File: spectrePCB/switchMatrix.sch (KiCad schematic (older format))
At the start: 256 parts

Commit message: finished capslock key and pin mapping. Rev1 done
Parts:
- added U?: TS3A24159DGSR, Package_SO:TSSOP-10_3x3mm_P0.5mm, symbol Analog_Switch:TS3A24159DGSR
- added U? (x2): 74LVC2G08, symbol 74xGxx:74LVC2G08
- added U?: CD74HC73M96, symbol MyComponents:CD74HC73M96
- MX?: value delete -> ctrl
- MX?: value menu -> del
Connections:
- net COL15 is gone; now on net COL13: MX?.1 (COL), MX?.1 (COL)
- net COL16 is gone; now on net COL14: MX?.1 (COL)
- net COL0: now also U?.1
- net COL10: now also MX?.1 (COL); no longer MX?.1 (COL)
- net COL11: now also MX?.1 (COL)
- net COL12: now also MX?.1 (COL), MX?.1 (COL), MX?.1 (COL); no longer MX?.1 (COL)
- net COL13: no longer MX?.1 (COL), MX?.1 (COL), MX?.1 (COL)
- net COL14: no longer MX?.1 (COL)
- net COL5: now also MX?.1 (COL)
- net COL6: no longer MX?.1 (COL)
- net COL9: now also MX?.1 (COL)
- net L+: now also U?.6; no longer R?.1
- net L-: no longer D?.1 (K), D?.1 (K), D?.1 (K), D?.1 (K), D?.1 (K), D?.1 (K), D?.1 (K), D?.1 (K), D?.1 (K), D?.1 (K), D?.1 (K), D?.1 (K), D?.1 (K)
- net ROW2: now also U?.2
- net at R?.2: now also U?.3; no longer D?.2 (A)
- new net: U?.7, U?.8
- new net: D?.2 (A), R?.1
- new net GND: U?.4 (GND), U?.4 (GND)
- new net ROW3: D?.1 (K), D?.1 (K), D?.1 (K), D?.1 (K), D?.1 (K), D?.1 (K), D?.1 (K), D?.1 (K), D?.1 (K), D?.1 (K), D?.1 (K), D?.1 (K), D?.1 (K)
- new net VCC: U?.8 (VCC), U?.8 (VCC)
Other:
- moved on the sheet: D?, MX?, R?

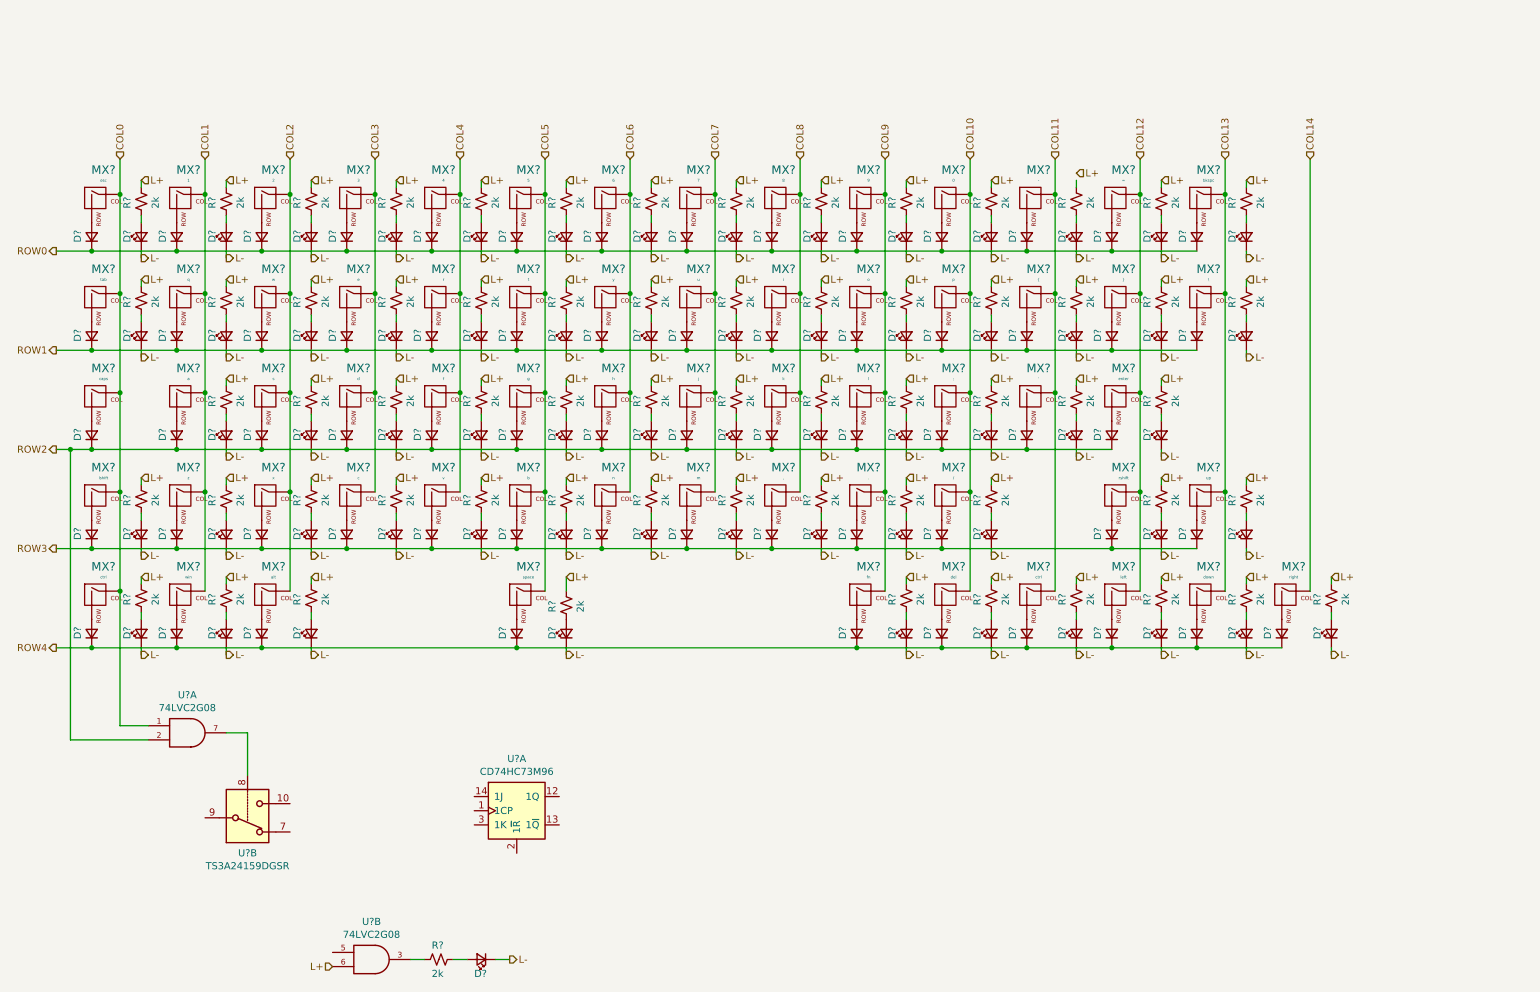
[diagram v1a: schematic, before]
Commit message: fixed big decoup cap not being big
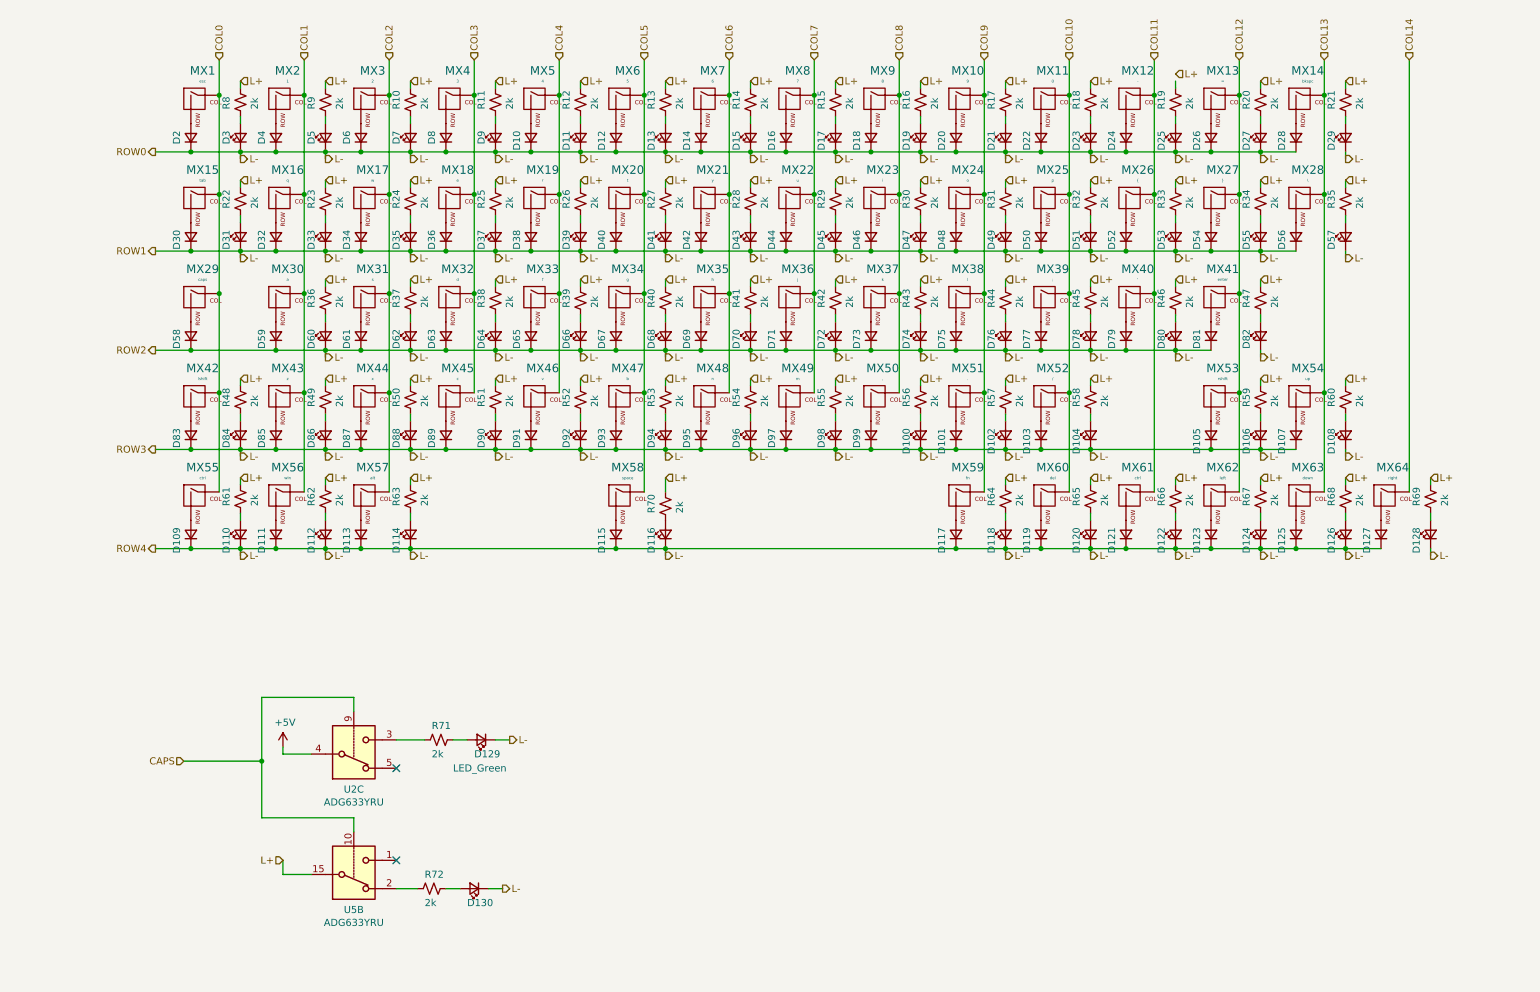
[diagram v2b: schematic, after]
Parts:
- removed U?: TS3A24159DGSR, Package_SO:TSSOP-10_3x3mm_P0.5mm, symbol Analog_Switch:TS3A24159DGSR
- removed U? (x2): 74LVC2G08, symbol 74xGxx:74LVC2G08
- removed U?: CD74HC73M96, symbol MyComponents:CD74HC73M96
- added D129: LED_Green, symbol Device:LED_Small
- added R71: 2k, symbol Device:R_Small_US
- added U2, U5: ADG633YRU, Package_SO:TSSOP-20_4.4x6.5mm_P0.65mm, symbol Analog_Switch:ADG633YRU
- gave numbers to parts that had none: 256
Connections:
- net ROW0 is gone; now on net L-: D10.1 (K), D12.1 (K), D14.1 (K), D16.1 (K), D18.1 (K), D2.1 (K), D20.1 (K), D22.1 (K), D24.1 (K), D26.1 (K), D28.1 (K), D4.1 (K), D6.1 (K), D8.1 (K)
- net ROW1 is gone; now on net L-: D30.1 (K), D32.1 (K), D34.1 (K), D36.1 (K), D38.1 (K), D40.1 (K), D42.1 (K), D44.1 (K), D46.1 (K), D48.1 (K), D50.1 (K), D52.1 (K), D54.1 (K), D56.1 (K)
- net ROW2 is gone; now on net L-: D58.1 (K), D59.1 (K), D61.1 (K), D63.1 (K), D65.1 (K), D67.1 (K), D69.1 (K), D71.1 (K), D73.1 (K), D75.1 (K), D77.1 (K), D79.1 (K), D81.1 (K)
- net ROW3 is gone; now on net L-: D101.1 (K), D103.1 (K), D105.1 (K), D107.1 (K), D83.1 (K), D85.1 (K), D87.1 (K), D89.1 (K), D91.1 (K), D93.1 (K), D95.1 (K), D97.1 (K), D99.1 (K)
- net ROW4 is gone; now on net L-: D109.1 (K), D111.1 (K), D113.1 (K), D115.1 (K), D117.1 (K), D119.1 (K), D121.1 (K), D123.1 (K), D125.1 (K), D127.1 (K)
- net L+: now also U5.15
- net L-: now also D129.1 (K)
- net at R72.2: now also U5.2
- new net: D129.2 (A), R71.1
- new net: R71.2, U2.3
- new net +5V: U2.4
- new net CAPS: U2.9, U5.10
- no-connect marks 0 -> 2
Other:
- moved on the sheet: D10, D100, D101, D102, D103, D104, D105, D106, D107, D108, D109, D11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

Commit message: added footprints to components
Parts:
- D10, D101, D103, D105, D107, D109, D111, D113, D115, D117, D119, D12, D121, D123, D125, D127, D14, D16, D18, D2, D20, D22, D24, D26, D28, D30, D32, D34, D36, D38, D4, D40, D42, D44, D46, D48, D50, D52, D54, D56, D58, D59, D6, D61, D63, D65, D67, D69, D71, D73, D75, D77, D79, D8, D81, D83, D85, D87, D89, D91, D93, D95, D97, D99: footprint (none) -> Diode_SMD:D_0603_1608Metric
- D100, D102, D104, D106, D108, D11, D110, D112, D114, D116, D118, D120, D122, D124, D126, D128, D129, D13, D130, D15, D17, D19, D21, D23, D25, D27, D29, D3, D31, D33, D35, D37, D39, D41, D43, D45, D47, D49, D5, D51, D53, D55, D57, D60, D62, D64, D66, D68, D7, D70, D72, D74, D76, D78, D80, D82, D84, D86, D88, D9, D90, D92, D94, D96, D98: footprint (none) -> LED_SMD:LED_0603_1608Metric
- MX1, MX10, MX11, MX12, MX13, MX16, MX17, MX18, MX19, MX2, MX20, MX21, MX22, MX23, MX24, MX25, MX26, MX27, MX3, MX30, MX31, MX32, MX33, MX34, MX35, MX36, MX37, MX38, MX39, MX4, MX40, MX43, MX44, MX45, MX46, MX47, MX48, MX49, MX5, MX50, MX51, MX52, MX54, MX6, MX62, MX63, MX64, MX7, MX8, MX9: footprint (none) -> MX_Alps_Hybrid:MX-1U-NoLED
- MX14: footprint (none) -> MX_Alps_Hybrid:MX-2U-NoLED
- MX15, MX28: footprint (none) -> MX_Alps_Hybrid:MX-1.5U-NoLED
- MX29: footprint (none) -> MX_Alps_Hybrid:MX-1.75U-NoLED
- MX41, MX42: footprint (none) -> MX_Alps_Hybrid:MX-2.25U-NoLED
- MX53: footprint (none) -> MX_Alps_Hybrid:MX-2.75U-NoLED
- MX55, MX56, MX57, MX59, MX60, MX61: footprint (none) -> MX_Alps_Hybrid:MX-1.25U-NoLED
- MX58: footprint (none) -> MX_Alps_Hybrid:MX-6.25U-NoLED
- R10, R11, R12, R13, R14, R15, R16, R17, R18, R19, R20, R21, R22, R23, R24, R25, R26, R27, R28, R29, R30, R31, R32, R33, R34, R35, R36, R37, R38, R39, R40, R41, R42, R43, R44, R45, R46, R47, R48, R49, R50, R51, R52, R53, R54, R55, R56, R57, R58, R59, R60, R61, R62, R63, R64, R65, R66, R67, R68, R69, R70, R71, R72, R8, R9: footprint (none) -> Resistor_SMD:R_0201_0603Metric

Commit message: dove into the rats nest. I regret everything
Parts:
- MX55: value ctrl -> ctrlL
- MX61: value ctrl -> ctrlR
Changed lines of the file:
@@
 P 8400 4250
 F 0 "MX61" H 8433 4473 60  0000 C CNN
-F 1 "ctrl" H 8433 4399 20  0000 C CNN
+F 1 "ctrlR" H 8433 4399 20  0000 C CNN
 F 2 "MX_Alps_Hybrid:MX-1.25U-NoLED" H 7775 4225 60  0001 C CNN
 F 3 "" H 7775 4225 60  0001 C CNN
@@
 P 1800 4250
 F 0 "MX55" H 1833 4473 60  0000 C CNN
-F 1 "ctrl" H 1833 4399 20  0000 C CNN
+F 1 "ctrlL" H 1833 4399 20  0000 C CNN
 F 2 "MX_Alps_Hybrid:MX-1.25U-NoLED" H 1175 4225 60  0001 C CNN
 F 3 "" H 1175 4225 60  0001 C CNN
@@
 	1    0    0    -1
 $EndComp
-Text HLabel 6900 2000 2    50   Input ~ 0
-L+
 Text HLabel 6900 2550 2    50   Output ~ 0
 L-
@@
 NoConn ~ 3200 6150
 NoConn ~ 3200 6800
+Text HLabel 6900 2000 2    50   Input ~ 0
+L+
 $EndSCHEMATC

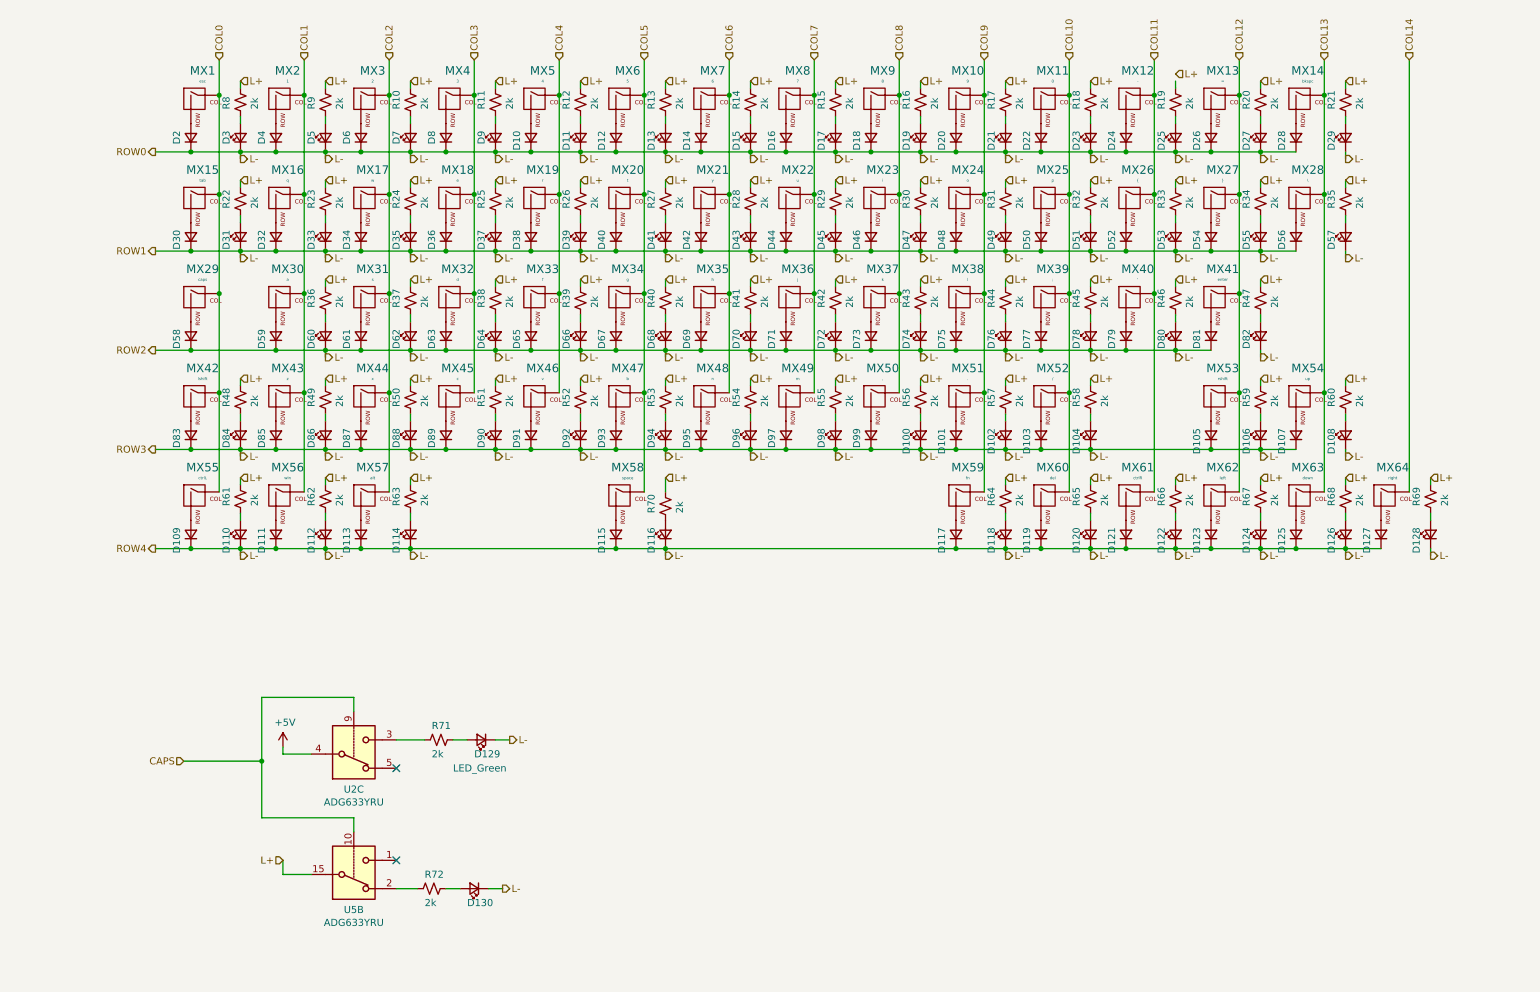
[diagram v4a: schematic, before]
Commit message: placed resistors, added edges, fixing GND net
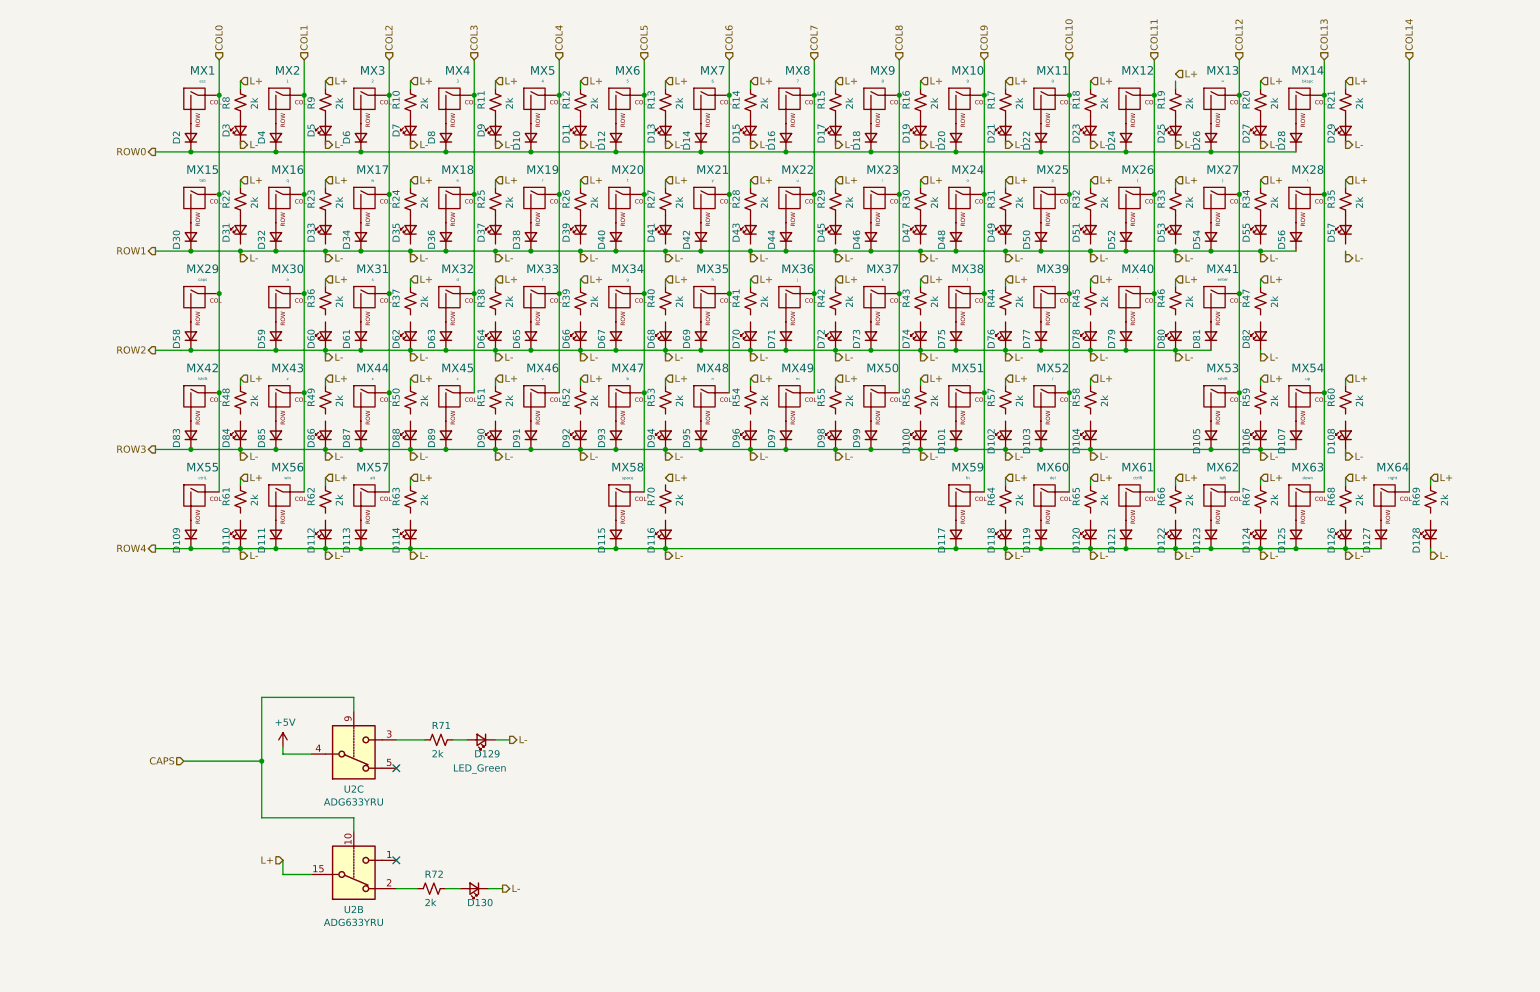
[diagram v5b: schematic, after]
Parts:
- R10, R11, R12, R13, R14, R15, R16, R17, R18, R19, R20, R21, R22, R23, R24, R25, R26, R27, R28, R29, R30, R31, R32, R33, R34, R35, R36, R37, R38, R39, R40, R41, R42, R43, R44, R45, R46, R47, R48, R49, R50, R51, R52, R53, R54, R55, R56, R57, R58, R59, R60, R61, R62, R63, R64, R65, R66, R67, R68, R69, R70, R71, R72, R8, R9: footprint Resistor_SMD:R_0201_0603Metric -> Resistor_SMD:R_0603_1608Metric
- renumbered U5 to U2
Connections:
- net L+: no longer R70.1
- net L-: no longer D10.1 (K), D12.1 (K), D14.1 (K), D16.1 (K), D18.1 (K), D2.1 (K), D20.1 (K), D22.1 (K), D24.1 (K), D26.1 (K), D28.1 (K), D31.1 (K), D33.1 (K), D35.1 (K), D37.1 (K), D39.1 (K), D4.1 (K), D41.1 (K), D43.1 (K), D45.1 (K), D47.1 (K), D49.1 (K), D51.1 (K), D53.1 (K), D55.1 (K), D57.1 (K), D6.1 (K), D8.1 (K)
- net at D84.2 (A): no longer R48.2
- net at D110.2 (A): no longer R61.2
- net at D60.2 (A): no longer R36.2
- net at D86.2 (A): no longer R49.2
- net at D112.2 (A): no longer R62.2
- net at D62.2 (A): no longer R37.2
- net at D88.2 (A): no longer R50.2
- net at D114.2 (A): no longer R63.2
- net at D64.2 (A): no longer R38.2
- net at D90.2 (A): no longer R51.2
- net at D66.2 (A): no longer R39.2
- net at D92.2 (A): no longer R52.2
- net at D68.2 (A): no longer R40.2
- net at D94.2 (A): no longer R53.2
- net at D70.2 (A): no longer R41.2
- net at D96.2 (A): no longer R54.2
- net at D116.2 (A): no longer R70.2
- net at D72.2 (A): no longer R42.2
- net at D98.2 (A): no longer R55.2
- net at D74.2 (A): no longer R43.2
- net at D100.2 (A): no longer R56.2
- net at D76.2 (A): no longer R44.2
- net at D102.2 (A): no longer R57.2
- net at D78.2 (A): no longer R45.2
- net at D104.2 (A): no longer R58.2
- net at D118.2 (A): no longer R64.2
- net at D80.2 (A): no longer R46.2
- net at D120.2 (A): no longer R65.2
- net at D82.2 (A): no longer R47.2
- net at D106.2 (A): no longer R59.2
- net at D122.2 (A): no longer R66.2
- net at D124.2 (A): no longer R67.2
- net at D108.2 (A): no longer R60.2
- net at D126.2 (A): no longer R68.2
- net at D128.2 (A): no longer R69.2
- new net ROW0: D10.1 (K), D12.1 (K), D14.1 (K), D16.1 (K), D18.1 (K), D2.1 (K), D20.1 (K), D22.1 (K), D24.1 (K), D26.1 (K), D28.1 (K), D4.1 (K), D6.1 (K), D8.1 (K)
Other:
- moved on the sheet: D11, D13, D15, D17, D19, D21, D23, D25, D27, D29, D3, D31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
